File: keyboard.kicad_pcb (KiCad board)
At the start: 2 copper layers, 313.6 x 138.6 mm, 120 parts, among them J1 USB_C_Receptacle_USB2.0_14P, J2 Conn_01x04, J3 Conn_01x04, J4 Conn_01x02, J6 Conn_01x02, SW1 SW_SPST, U1 nRF52840, U3 MCP73811T-420I-OT, X1 32MHz, X2 32.768kHz

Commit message: Start routing antennna
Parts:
- removed C18: 4.7uF, Capacitor_SMD:C_0603_1608Metric
- removed R3: 5k, Resistor_SMD:R_0603_1608Metric
- removed R4: 10k, Resistor_SMD:R_0603_1608Metric
- removed SW1: SW_SPST, Button_Switch_SMD:SW_SPDT_PCM12
- removed U3: MCP73811T-420I-OT, Package_TO_SOT_SMD:SOT-23-5
- added U2: BQ24075RGT, Package_DFN_QFN:VQFN-16-1EP_3x3mm_P0.5mm_EP1.6x1.6mm, F.Cu at (349.1, 230.5)
- AE1: footprint RF_Antenna:Texas_SWRA117D_2.4GHz_Left -> RF_Antenna:Texas_SWRA117D_2.4GHz_Right; moved to F.Cu
- C16, J1, L2, L3, U1: moved to F.Cu
- L1: footprint Inductor_SMD:L_6.3x6.3_H3 -> Inductor_SMD:L_0603_1608Metric; moved to F.Cu
- moved J4 187.9 mm to (358.1, 221.0)
- moved J1 174.9 mm to (361.6, 213.9), turned to 180 degrees
- moved R1 160.3 mm to (348.4, 222.0)
- moved R2 160.0 mm to (348.4, 224.5)
- moved J6 155.0 mm to (362.7, 221.0), turned to 0 degrees
- moved J2 154.9 mm to (348.8, 210.8)
- moved X1 131.8 mm to (340.5, 211.1), turned to 0 degrees
- moved C17 131.4 mm to (334.6, 214.8), turned to 0 degrees
- moved C14 128.8 mm to (330.6, 224.8), turned to 0 degrees
- moved J3 126.8 mm to (353.4, 210.8), turned to 0 degrees
- moved X2 123.8 mm to (340.5, 216.1), turned to 0 degrees
- moved C1 120.8 mm to (326.6, 209.8), turned to 0 degrees
- moved C10 118.4 mm to (330.6, 214.8)
- moved C9 118.4 mm to (330.6, 212.3)
- moved C8 118.4 mm to (330.6, 209.8)
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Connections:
- net /Controller/VDD_HV renamed VDDH
- C10 pad 1: VEXT -> VDD
- C5 pad 1: VEXT -> VDD
- C7 pad 1: VEXT -> VDD
- C8 pad 1: VEXT -> VDD
- C9 pad 1: VEXT -> VDD
- J3 pad 2: VBUS -> VDD
- J4 pad 1: Net-(J4-Pin_1) -> VBAT
- L1 pad 2: VEXT -> VDD
- U1 pad A22: VEXT -> VDD
- U1 pad AD14: VEXT -> VDD
- U1 pad AD23: VEXT -> VDD
- U1 pad B1: VEXT -> VDD
- U1 pad W1: VEXT -> VDD
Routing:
- net GND: track 289.9 -> 9.87 mm, vias 5 -> 0
- net VBUS: track 165.3 -> 0.00 mm, vias 9 -> 0
- net COL4: track 381.4 -> 247.1 mm, vias 7 -> 2
- net USBD-: track 99.1 -> 0.00 mm, vias 3 -> 0
- net USBD+: track 96.6 -> 0.00 mm, vias 4 -> 0
- net Net-(U1-ANT): track 94.1 -> 4.54 mm, vias 1 -> 0
- net BAT_STATE: track 80.8 -> 0.00 mm, vias 3 -> 0
- net COL5: track 292.2 -> 216.9 mm, vias 4 -> 2
- net COL3: track 351.2 -> 276.0 mm, vias 4 -> 2
- net COL1: track 520.1 -> 453.7 mm, vias 4 -> 2
- net COL0: track 529.2 -> 463.1 mm, vias 4 -> 2
- net COL2: track 413.0 -> 348.1 mm, vias 5 -> 3
- net VEXT: track 49.0 -> 0.00 mm, vias 3 -> 0
- net SWD: track 19.6 -> 0.00 mm
- net SWC: track 18.0 -> 0.00 mm
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
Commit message: Change board shape
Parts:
- added Q1: 2N7002, Package_TO_SOT_SMD:SOT-23, F.Cu at (231.8, 204.8)
- AE1: footprint RF_Antenna:Texas_SWRA117D_2.4GHz_Right -> RF_Antenna:Texas_SWRA117D_2.4GHz_Left
- moved J1 307.5 mm to (68.2, 121.8), turned to -90 degrees
- moved J2 142.3 mm to (209.8, 180.2)
- moved R1 142.3 mm to (209.5, 191.4)
- moved R2 142.3 mm to (209.5, 193.9)
- moved J3 142.3 mm to (214.5, 180.2)
- moved J4 142.3 mm to (219.1, 190.4)
- moved J6 142.3 mm to (223.8, 190.4)
- moved L1 122.7 mm to (217.5, 206.0)
- moved U2 121.0 mm to (232.0, 199.9)
- moved C1 117.6 mm to (209.5, 198.5)
- moved C17 117.6 mm to (217.5, 203.5)
- moved C2 117.6 mm to (209.5, 201.0)
- moved C3 117.6 mm to (209.5, 203.5)
- moved C4 117.6 mm to (209.5, 206.0)
- moved C5 117.6 mm to (209.5, 208.5)
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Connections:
- U1 pad A12: BAT_STATE -> unconnected-(U1-AIN0/P0.02-PadA12)
- U1 pad AD10: COL5 -> unconnected-(U1-P0.15-PadAD10)
- U1 pad AD12: COL4 -> unconnected-(U1-P0.17-PadAD12)
- U1 pad AD8: COL3 -> unconnected-(U1-P0.13-PadAD8)
- U1 pad G1: ROW6 -> unconnected-(U1-P0.26-PadG1)
- U1 pad J1: ROW5 -> unconnected-(U1-AIN2/P0.04-PadJ1)
- U1 pad J24: COL0 -> unconnected-(U1-NFC2/P0.10-PadJ24)
- U1 pad L1: ROW4 -> unconnected-(U1-P0.06-PadL1)
- U1 pad L24: COL1 -> unconnected-(U1-NFC1/P0.09-PadL24)
- U1 pad N1: ROW3 -> unconnected-(U1-P0.08-PadN1)
- U1 pad R24: ROW2 -> unconnected-(U1-P1.06-PadR24)
- U1 pad U1: COL2 -> unconnected-(U1-TRACEDATA1/P0.12-PadU1)
- U1 pad U24: ROW1 -> unconnected-(U1-P1.04-PadU24)
- U1 pad W24: ROW0 -> unconnected-(U1-P1.02-PadW24)
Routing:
- net COL0: track 463.1 -> 76.0 mm, vias 2 -> 0
- net COL1: track 453.7 -> 76.0 mm, vias 2 -> 0
- net COL2: track 348.1 -> 57.0 mm, vias 3 -> 0
- net ROW3: track 231.2 -> 0.00 mm, vias 5 -> 0
- net COL3: track 276.0 -> 76.0 mm, vias 2 -> 0
- net COL4: track 247.1 -> 76.0 mm, vias 2 -> 0
- net COL5: track 216.9 -> 76.0 mm, vias 2 -> 0
- net ROW6: track 195.0 -> 111.0 mm
- net ROW2: track 186.4 -> 113.1 mm
- net ROW5: track 178.3 -> 107.9 mm
- net ROW4: track 169.9 -> 105.1 mm
- net ROW1: track 169.3 -> 110.3 mm
- net ROW0: track 164.2 -> 107.8 mm
- net Net-(D40-A): track 14.5 -> 0.00 mm
- net Net-(D21-A): track 13.8 -> 0.00 mm
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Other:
- board size 313.6 x 138.6 mm -> 314.7 x 144.5 mm

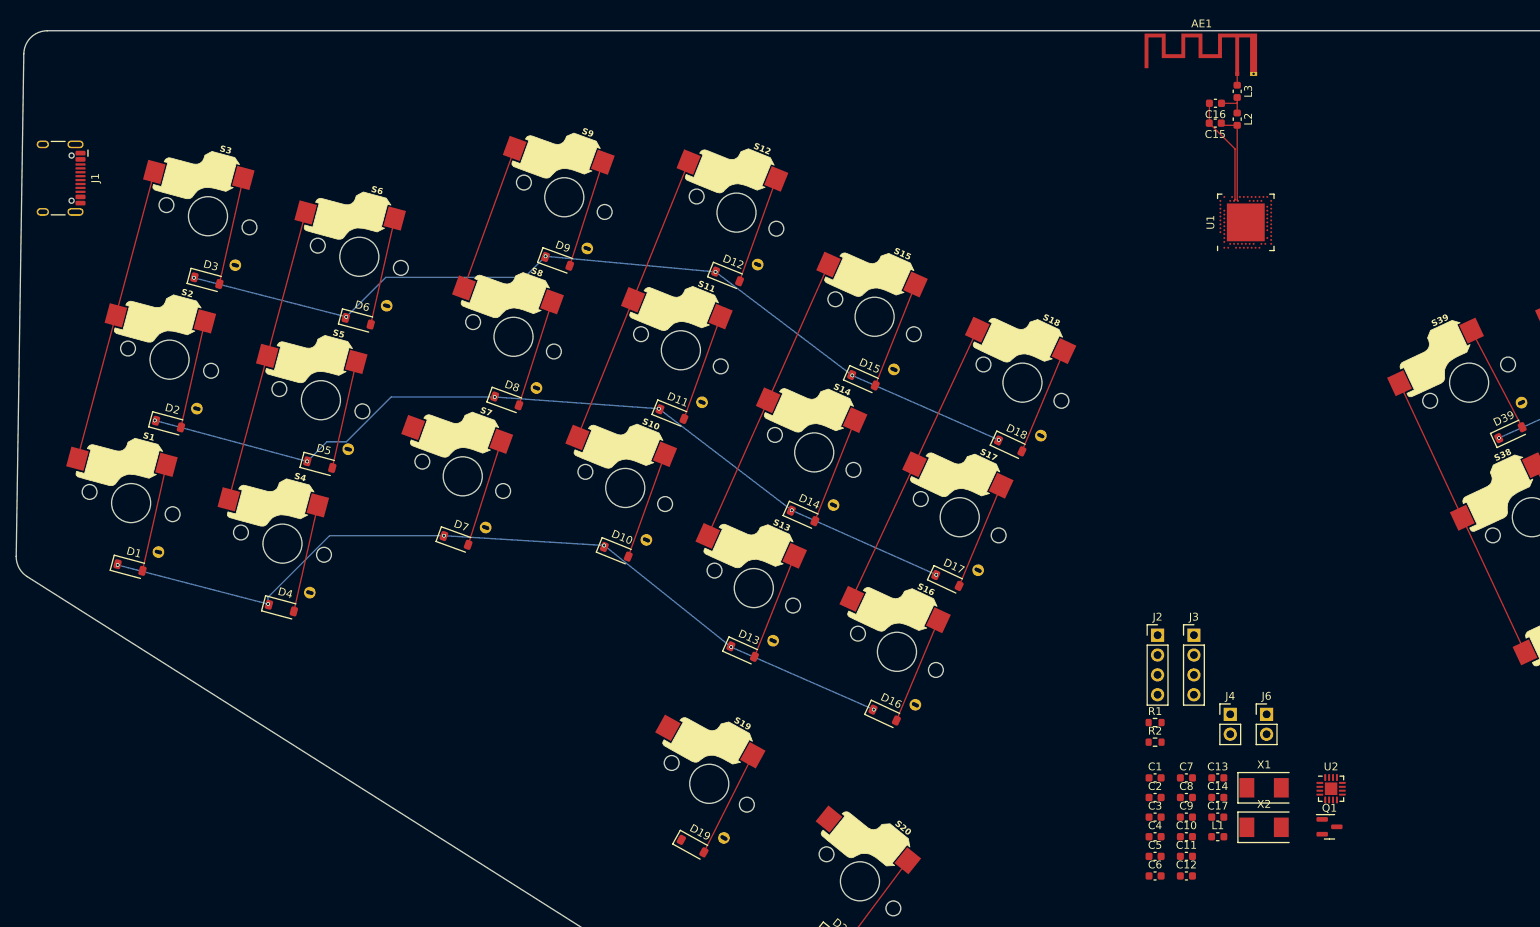
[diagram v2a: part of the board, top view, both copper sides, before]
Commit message: Route CPU and charging circuit
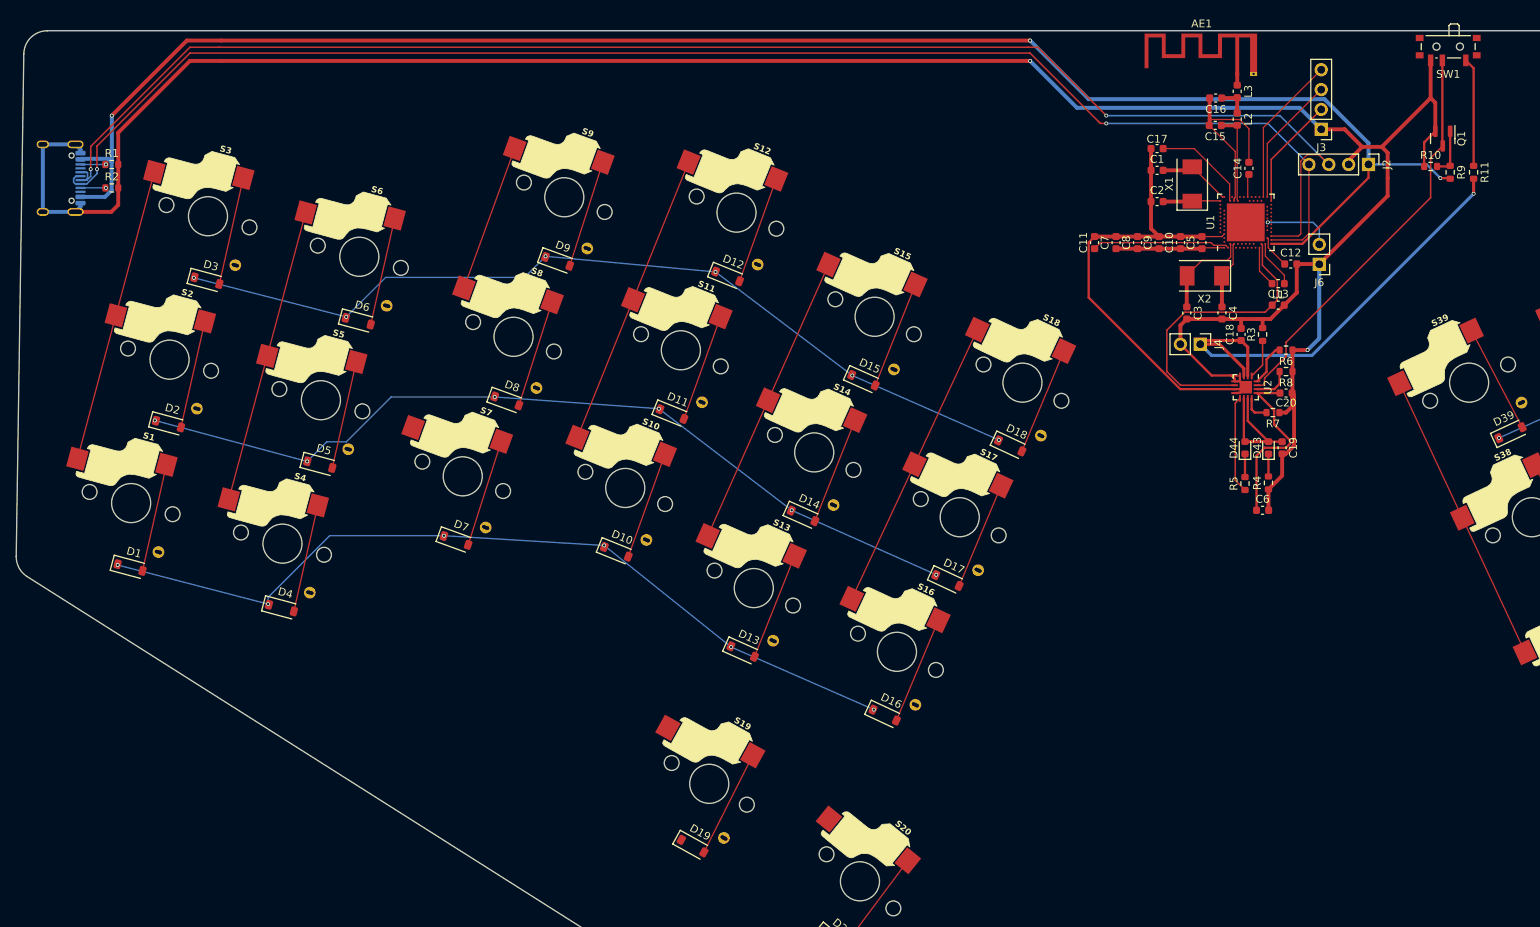
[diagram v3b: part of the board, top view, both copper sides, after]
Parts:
- added C18: 4.7uF, Capacitor_SMD:C_0603_1608Metric, F.Cu at (220.5, 141.8)
- added C19: 4.7uF, Capacitor_SMD:C_0603_1608Metric, F.Cu at (225.8, 156.2)
- added C20: 4.7uF, Capacitor_SMD:C_0603_1608Metric, F.Cu at (226.2, 149.2)
- added D43: LED_PGOOD, LED_SMD:LED_0603_1608Metric, F.Cu at (224.0, 156.2)
- added D44: LED_CHARGE, LED_SMD:LED_0603_1608Metric, F.Cu at (221.0, 156.2)
- added R10: 10k, Resistor_SMD:R_0603_1608Metric, F.Cu at (244.8, 120.2)
- added R11: 100k, Resistor_SMD:R_0603_1608Metric, F.Cu at (250.2, 121.0)
- added R3: 10k, Resistor_SMD:R_0603_1608Metric, F.Cu at (223.2, 141.8)
- added R4: 1.5k, Resistor_SMD:R_0603_1608Metric, F.Cu at (224.0, 160.8)
- added R5: 1.5k, Resistor_SMD:R_0603_1608Metric, F.Cu at (221.0, 160.8)
- added R6: 3.9k, Resistor_SMD:R_0603_1608Metric, F.Cu at (226.2, 143.8)
- added R7: 1.5k, Resistor_SMD:R_0603_1608Metric, F.Cu at (224.6, 151.8)
- added R8: 47k, Resistor_SMD:R_0603_1608Metric, F.Cu at (226.2, 146.5)
- added R9: 100, Resistor_SMD:R_0603_1608Metric, F.Cu at (247.2, 121.0)
- added SW1: SW_SPDT, Button_Switch_SMD:SW_SPDT_PCM12, F.Cu at (247.0, 105.2)
- J1: moved to B.Cu
- moved R1 151.4 mm to (76.0, 120.0)
- moved R2 151.2 mm to (76.0, 123.0)
- moved Q1 89.2 mm to (246.3, 116.7), turned to -90 degrees
- moved C17 85.9 mm to (209.8, 118.0), turned to 180 degrees
- moved C14 80.6 mm to (221.5, 120.5), turned to 90 degrees
- moved C12 79.4 mm to (226.8, 132.7)
- moved C11 79.4 mm to (201.8, 130.0), turned to 90 degrees
- moved C5 78.8 mm to (215.5, 130.0), turned to 90 degrees
- moved X1 77.8 mm to (214.2, 122.5), turned to 90 degrees
- moved C1 77.7 mm to (209.8, 120.8)
- moved C2 76.3 mm to (209.8, 124.8)
- moved C10 76.0 mm to (212.8, 130.0), turned to 90 degrees
- moved C9 73.6 mm to (210.0, 130.0), turned to 90 degrees
- moved C8 71.3 mm to (207.2, 130.0), turned to 90 degrees
- moved L1 71.2 mm to (225.2, 135.2), turned to 180 degrees
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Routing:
- net GND: track 14.3 -> 418.5 mm, vias 0 -> 2
- net VBUS: track 0.00 -> 243.0 mm, vias 0 -> 3
- net USBD+: track 0.00 -> 195.5 mm, vias 0 -> 2
- net USBD-: track 0.00 -> 188.5 mm, vias 0 -> 2
- net VBAT: track 0.00 -> 64.2 mm, vias 0 -> 1
- net VDDH: track 0.00 -> 55.4 mm
- net SYSOFF: track 0.00 -> 52.0 mm
- net VDD: track 0.00 -> 33.5 mm
- net SWC: track 0.00 -> 19.3 mm
- net Net-(U1-DEC1): track 0.00 -> 17.7 mm
- net SWD: track 0.00 -> 16.6 mm
- net Net-(SW1-A): track 0.00 -> 13.9 mm
- net Net-(U1-DEC3): track 0.00 -> 12.6 mm
- net Net-(U2-~{CHG}): track 0.00 -> 12.5 mm
- net Net-(U1-XL1/P0.00): track 0.00 -> 12.3 mm
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
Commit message: Route rows and columns
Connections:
- U1 pad A10: unconnected-(U1-AIN5/P0.29-PadA10) -> COL1
- U1 pad A12: unconnected-(U1-AIN0/P0.02-PadA12) -> COL2
- U1 pad A14: unconnected-(U1-P1.15-PadA14) -> COL3
- U1 pad A16: unconnected-(U1-P1.13-PadA16) -> COL4
- U1 pad A20: unconnected-(U1-P1.10-PadA20) -> COL5
- U1 pad A8: unconnected-(U1-AIN7/P0.31-PadA8) -> COL0
- U1 pad AD20: unconnected-(U1-P0.24-PadAD20) -> ROW6
- U1 pad AD22: unconnected-(U1-TRACEDATA0/P1.00-PadAD22) -> ROW5
- U1 pad J24: unconnected-(U1-NFC2/P0.10-PadJ24) -> ROW2
- U1 pad L24: unconnected-(U1-NFC1/P0.09-PadL24) -> ROW1
- U1 pad R24: unconnected-(U1-P1.06-PadR24) -> ROW0
- U1 pad U24: unconnected-(U1-P1.04-PadU24) -> ROW3
- U1 pad W24: unconnected-(U1-P1.02-PadW24) -> ROW4
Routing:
- net COL2: track 57.0 -> 597.1 mm, vias 0 -> 6
- net COL0: track 76.0 -> 534.8 mm, vias 0 -> 4
- net COL3: track 76.0 -> 503.9 mm, vias 0 -> 6
- net COL1: track 76.0 -> 501.8 mm, vias 0 -> 4
- net COL4: track 76.0 -> 411.3 mm, vias 0 -> 6
- net ROW3: track 0.00 -> 324.0 mm, vias 0 -> 2
- net COL5: track 76.0 -> 347.2 mm, vias 0 -> 2
- net ROW4: track 105.1 -> 213.7 mm, vias 6 -> 8
- net ROW0: track 107.8 -> 210.9 mm, vias 6 -> 7
- net ROW1: track 110.3 -> 199.8 mm, vias 6 -> 7
- net ROW5: track 107.9 -> 178.1 mm, vias 6 -> 7
- net ROW2: track 113.1 -> 177.6 mm, vias 6 -> 7
- net ROW6: track 111.0 -> 159.1 mm, vias 6 -> 7
- net Net-(D40-A): track 0.00 -> 14.2 mm
- net Net-(D41-A): track 0.00 -> 13.9 mm
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
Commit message: Add ground fill
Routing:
- net COL3: track 503.9 -> 505.1 mm
- net GND: vias 2 -> 146
- added copper zone on B.Cu, net GND
- added copper zone on F.Cu, net GND

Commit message: Change board shape
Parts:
- moved J1 39.3 mm to (106.8, 113.8), turned to 3.8 degrees
- moved R1 33.1 mm to (109.0, 121.4), turned to -86.2 degrees
- moved R2 30.1 mm to (106.0, 121.6), turned to -86.2 degrees
- moved SW1 11.6 mm to (258.0, 108.8), turned to 173.5 degrees
- moved Q1 7.52 mm to (246.8, 124.2)
- moved R10 7.52 mm to (245.2, 127.8)
- moved R11 7.52 mm to (250.8, 128.5)
- moved R9 7.52 mm to (247.8, 128.5)
- moved J3 6.00 mm to (236.8, 115.5), turned to -90 degrees
- moved AE1 1.10 mm to (220.0, 109.5)
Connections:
- J3 pad 1: GND -> VDD
- J3 pad 2: VDD -> GND
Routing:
- net COL5: track 347.2 -> 264.5 mm
- net COL4: track 411.3 -> 460.9 mm
- net COL3: track 505.1 -> 553.3 mm
- net USBD+: track 195.5 -> 154.6 mm, vias 2 -> 4
- net VBUS: track 242.9 -> 203.2 mm, vias 3 -> 1
- net USBD-: track 188.5 -> 149.5 mm, vias 2 -> 4
- net COL2: track 597.1 -> 628.0 mm
- net COL1: track 501.8 -> 524.8 mm
- net GND: track 416.3 -> 400.1 mm, vias 146 -> 24
- net COL0: track 534.8 -> 550.9 mm
- net SWC: track 19.3 -> 11.1 mm
- net ROW5: track 178.1 -> 186.2 mm
- net ROW1: track 199.8 -> 192.0 mm
- net Net-(SW1-A): track 13.9 -> 21.1 mm
- net SYSOFF: track 51.9 -> 58.7 mm
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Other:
- board size 314.7 x 144.5 mm -> 313.2 x 143.5 mm
- board text added: "BAT (- +)"
- board text added: "DBG (SWC SWD G V)"
- board text added: "RST"
- board text added: "USB (D- D+ G V)"

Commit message: first jlc submission
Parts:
- removed X1: 32MHz, Crystal:Crystal_SMD_0603-2Pin_6.0x3.5mm
- added Y1: 32MHz, Crystal:Crystal_SMD_2016-4Pin_2.0x1.6mm, F.Cu at (213.2, 122.8)
- SW1: moved to B.Cu
- X2: footprint Crystal:Crystal_SMD_0603-2Pin_6.0x3.5mm -> Crystal:Crystal_SMD_3215-2Pin_3.2x1.5mm
- moved C17 2.59 mm to (209.8, 120.6)
- moved C1 1.31 mm to (209.8, 122.1)
- moved C2 1.19 mm to (209.8, 123.6)
- moved C4 1.03 mm to (217.0, 139.0)
- moved C3 0.97 mm to (214.5, 139.0)
- turned SW1 to -6.5 degrees
- turned X2 to 0 degrees
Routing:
- net VBUS: track 203.2 -> 223.5 mm, vias 1 -> 3
- net GND: track 400.1 -> 414.1 mm, vias 24 -> 32
- net VBAT: track 59.8 -> 63.6 mm
- net SYSOFF: track 58.7 -> 61.8 mm, vias 0 -> 1
- net Net-(U1-DEC3): track 12.6 -> 10.4 mm
- net Net-(U1-XC2): track 7.23 -> 8.45 mm
- net Net-(U1-XL2/P0.01): track 8.68 -> 9.30 mm
- net Net-(SW1-A): track 21.1 -> 20.7 mm, vias 0 -> 1
- net ROW2: vias 8 -> 7
